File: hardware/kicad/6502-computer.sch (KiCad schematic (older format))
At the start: 35 parts, among them J1 Conn_02x20_Odd_Even, J2 Barrel_Jack, J3 Conn_02x02_Odd_Even, J4 Conn_02x06_Odd_Even, J5 Conn_02x06_Odd_Even, J6 Conn_01x06_Female, SW1 SW_SPDT, SW2 SW_SPDT, SW3 SW_Push, U1 W65C02SxP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

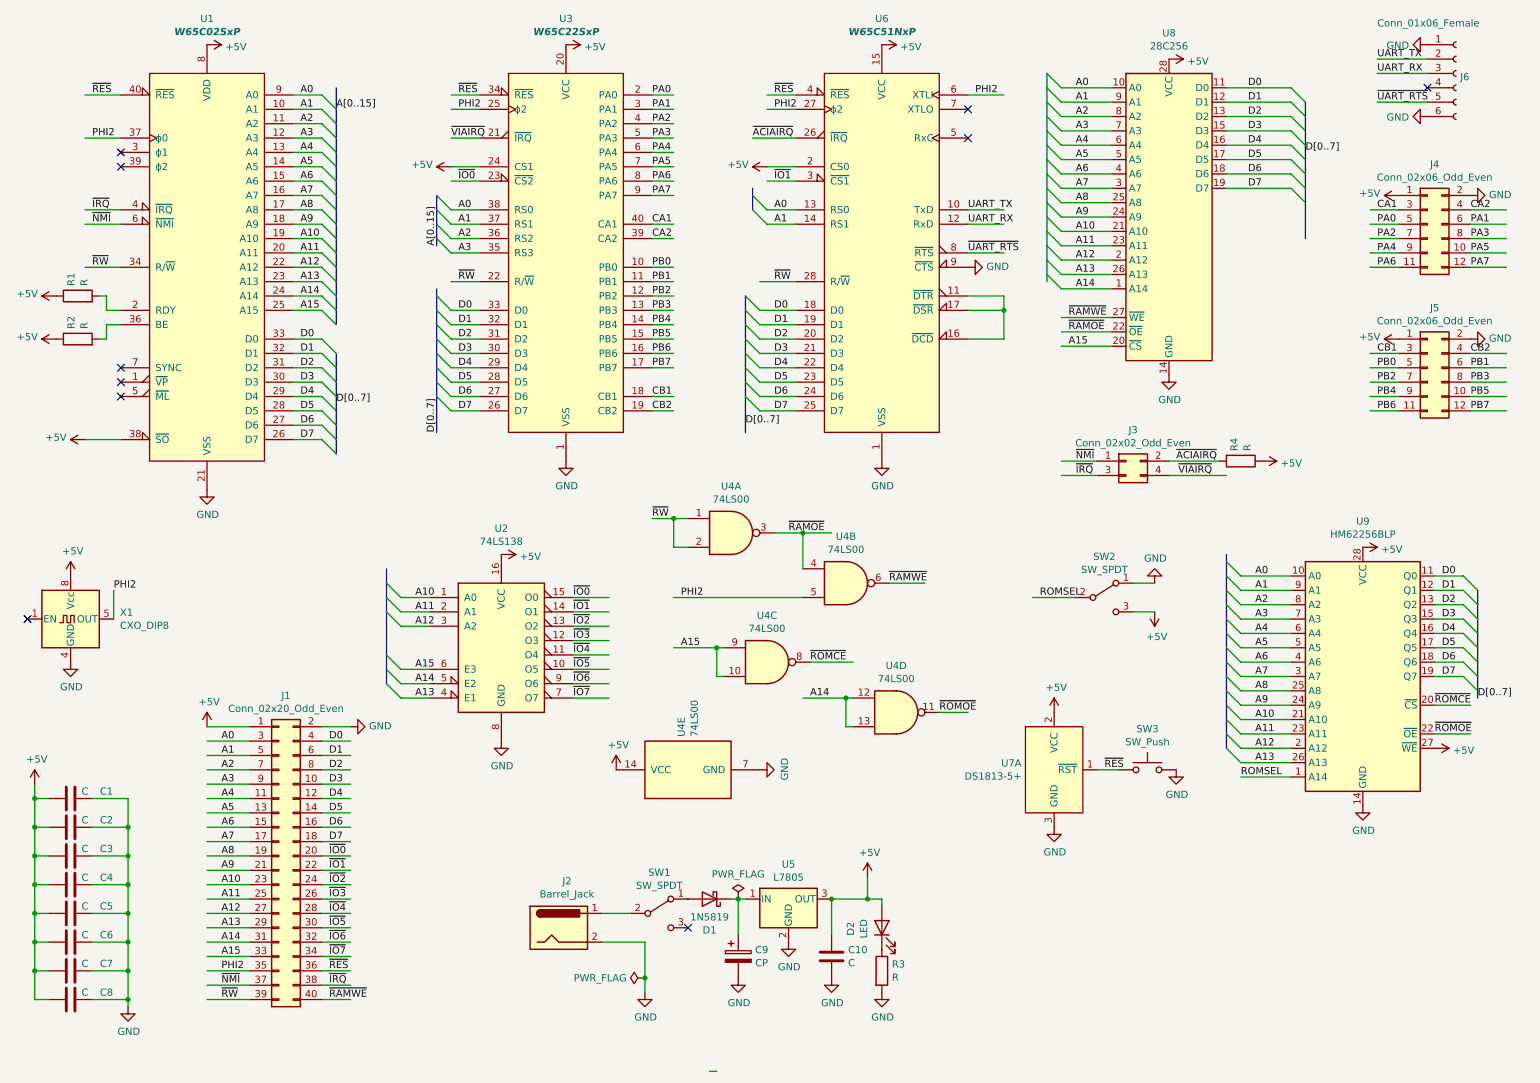
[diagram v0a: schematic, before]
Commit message: add component values
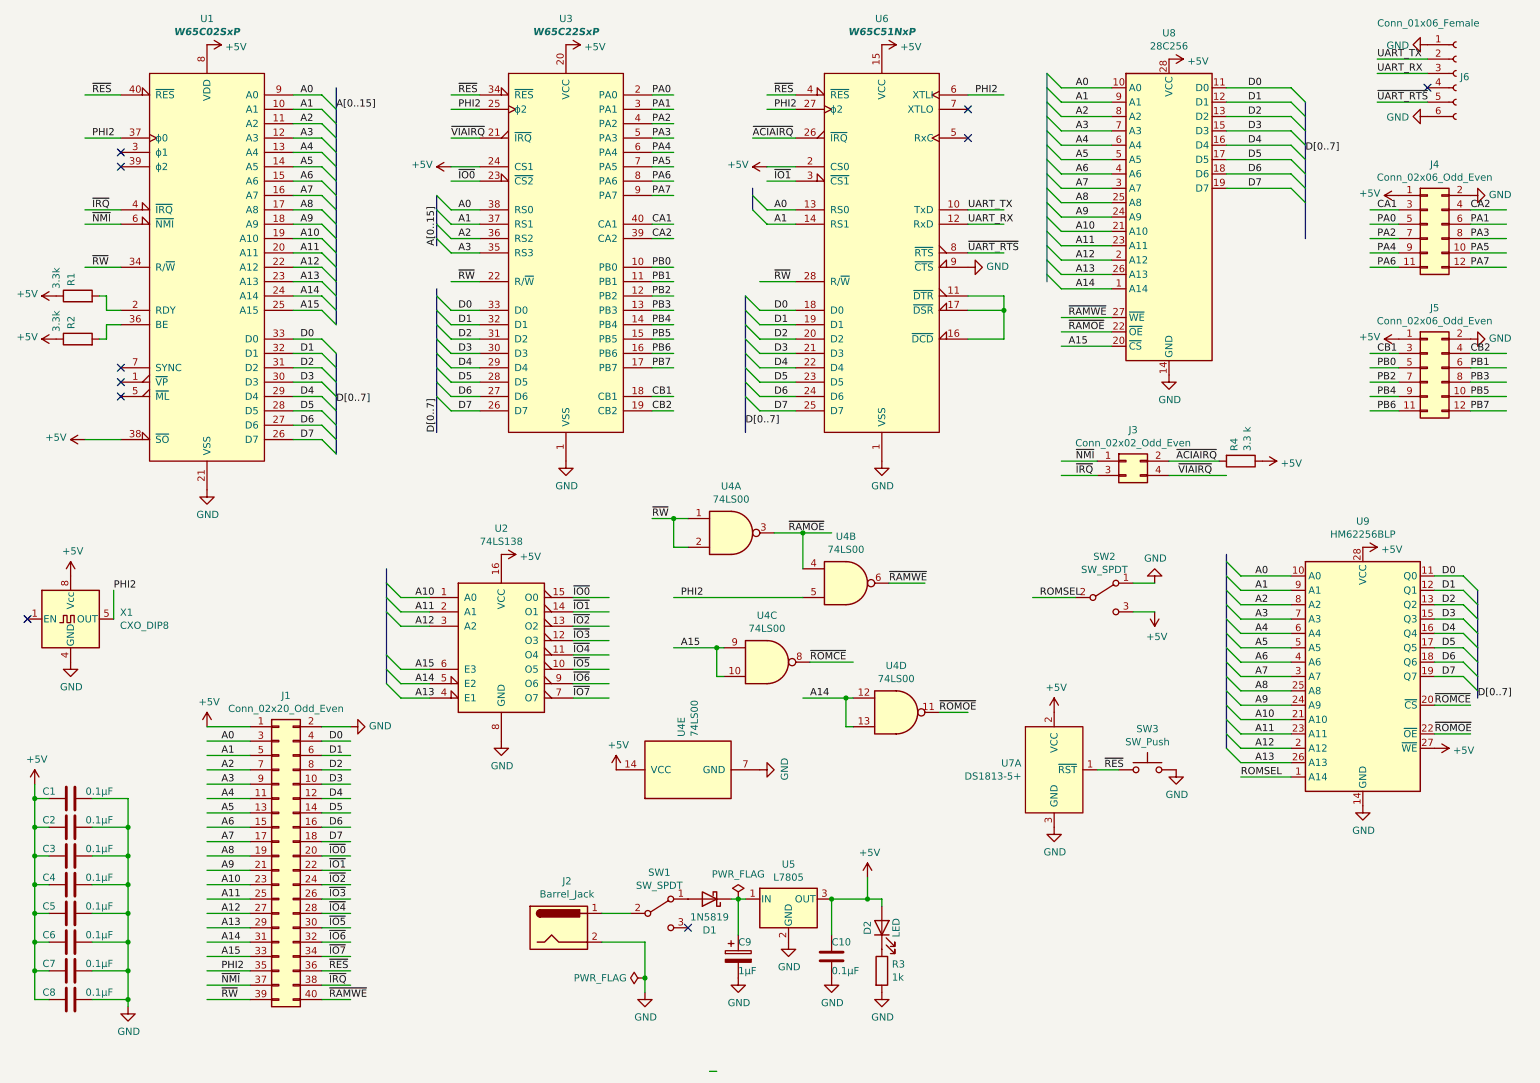
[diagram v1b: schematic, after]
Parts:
- C1, C10, C2, C3, C4, C5, C6, C7, C8: value C -> 0.1µF
- C9: value CP -> 1µF
- R1, R2: value R -> 3.3k
- R3: value R -> 1k
- R4: value R -> 3.3 k
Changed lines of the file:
@@
 U 1 1 61089D2F
 P 6250 7100
-F 0 "C10" H 6365 7146 50  0000 L CNN
-F 1 "C" H 6365 7055 50  0000 L CNN
+F 0 "C10" H 6250 7200 50  0000 L CNN
+F 1 "0.1µF" H 6250 7000 50  0000 L CNN
 F 2 "Capacitor_THT:C_Disc_D5.0mm_W2.5mm_P2.50mm" H 6288 6950 50  0001 C CNN
 F 3 "~" H 6250 7100 50  0001 C CNN
@@
 U 1 1 612507AF
 P 6600 6900
-F 0 "D2" H 6593 7117 50  0000 C CNN
-F 1 "LED" H 6593 7026 50  0000 C CNN
+F 0 "D2" H 6600 7000 50  0000 C CNN
+F 1 "LED" H 6600 6800 50  0000 C CNN
 F 2 "LED_THT:LED_D5.0mm" H 6600 6900 50  0001 C CNN
 F 3 "~" H 6600 6900 50  0001 C CNN
@@
 P 6600 7200
 F 0 "R3" H 6670 7246 50  0000 L CNN
-F 1 "R" H 6670 7155 50  0000 L CNN
+F 1 "1k" H 6670 7155 50  0000 L CNN
 F 2 "Resistor_THT:R_Axial_DIN0207_L6.3mm_D2.5mm_P10.16mm_Horizontal" V 6530 7200 50  0001 C CNN
 F 3 "~" H 6600 7200 50  0001 C CNN
@@
 P 1000 2800
 F 0 "R2" H 1070 2846 50  0000 L CNN
-F 1 "R" H 1070 2755 50  0000 L CNN
+F 1 "3.3k" H 1050 2950 50  0000 L CNN
 F 2 "Resistor_THT:R_Axial_DIN0207_L6.3mm_D2.5mm_P10.16mm_Horizontal" V 930 2800 50  0001 C CNN
 F 3 "~" H 1000 2800 50  0001 C CNN
@@
 P 1000 2500
 F 0 "R1" H 1070 2546 50  0000 L CNN
-F 1 "R" H 1070 2455 50  0000 L CNN
+F 1 "3.3k" H 1050 2650 50  0000 L CNN
 F 2 "Resistor_THT:R_Axial_DIN0207_L6.3mm_D2.5mm_P10.16mm_Horizontal" V 930 2500 50  0001 C CNN
 F 3 "~" H 1000 2500 50  0001 C CNN
@@
 ~ACIAIRQ
 $Comp
-L Device:R R4
-U 1 1 6218038F
-P 9100 3650
-F 0 "R4" H 9030 3604 50  0000 R CNN
-F 1 "R" H 9030 3695 50  0000 R CNN
-F 2 "Resistor_THT:R_Axial_DIN0207_L6.3mm_D2.5mm_P10.16mm_Horizontal" V 9030 3650 50  0001 C CNN
-F 3 "~" H 9100 3650 50  0001 C CNN
-	1    9100 3650
-	0    1    1    0
-$EndComp
-$Comp
 L Connector_Generic:Conn_02x02_Odd_Even J3
 U 1 1 62141DBF
@@
 $EndComp
 $Comp
-L power:GND #PWR0141
-U 1 1 62A2C16E
-P 1350 7450
-F 0 "#PWR0141" H 1350 7200 50  0001 C CNN
-F 1 "GND" H 1355 7277 50  0000 C CNN
-F 2 "" H 1350 7450 50  0001 C CNN
-F 3 "" H 1350 7450 50  0001 C CNN
-	1    1350 7450
-	1    0    0    -1
-$EndComp
-$Comp
-L Device:C C1
-U 1 1 62A8A6E5
-P 950 6000
-F 0 "C1" V 900 6250 50  0000 C CNN
-F 1 "C" V 900 6100 50  0000 C CNN
-F 2 "Capacitor_THT:C_Disc_D5.0mm_W2.5mm_P2.50mm" H 988 5850 50  0001 C CNN
-F 3 "~" H 950 6000 50  0001 C CNN
-	1    950  6000
-	0    1    1    0
-$EndComp
-$Comp
-L Device:C C2
-U 1 1 62AEDE99
-P 950 6200
-F 0 "C2" V 900 6450 50  0000 C CNN
-F 1 "C" V 900 6300 50  0000 C CNN
-F 2 "Capacitor_THT:C_Disc_D5.0mm_W2.5mm_P2.50mm" H 988 6050 50  0001 C CNN
-F 3 "~" H 950 6200 50  0001 C CNN
-	1    950  6200
-	0    1    1    0
-$EndComp
-$Comp
-L Device:C C4
-U 1 1 62BCA622
-P 950 6600
-F 0 "C4" V 900 6850 50  0000 C CNN
-F 1 "C" V 900 6700 50  0000 C CNN
-F 2 "Capacitor_THT:C_Disc_D5.0mm_W2.5mm_P2.50mm" H 988 6450 50  0001 C CNN
-F 3 "~" H 950 6600 50  0001 C CNN
-	1    950  6600
-	0    1    1    0
-$EndComp
-$Comp
 L Device:C C5
 U 1 1 62BCB673
 P 950 6800
-F 0 "C5" V 900 7050 50  0000 C CNN
-F 1 "C" V 900 6900 50  0000 C CNN
+F 0 "C5" V 900 6650 50  0000 C CNN
+F 1 "0.1µF" V 900 7000 50  0000 C CNN
 F 2 "Capacitor_THT:C_Disc_D5.0mm_W2.5mm_P2.50mm" H 988 6650 50  0001 C CNN
 F 3 "~" H 950 6800 50  0001 C CNN
@@
 U 1 1 62BCC41D
 P 950 7000
-F 0 "C6" V 900 7250 50  0000 C CNN
-F 1 "C" V 900 7100 50  0000 C CNN
+F 0 "C6" V 900 6850 50  0000 C CNN
+F 1 "0.1µF" V 900 7200 50  0000 C CNN
 F 2 "Capacitor_THT:C_Disc_D5.0mm_W2.5mm_P2.50mm" H 988 6850 50  0001 C CNN
 F 3 "~" H 950 7000 50  0001 C CNN
@@
 $EndComp
 $Comp
-L Device:C C7
-U 1 1 62BCD16B
-P 950 7200
-F 0 "C7" V 900 7450 50  0000 C CNN
-F 1 "C" V 900 7300 50  0000 C CNN
-F 2 "Capacitor_THT:C_Disc_D5.0mm_W2.5mm_P2.50mm" H 988 7050 50  0001 C CNN
-F 3 "~" H 950 7200 50  0001 C CNN
-	1    950  7200
-	0    1    1    0
-$EndComp
-$Comp
 L Device:C C8
 U 1 1 62BEB99E
 P 950 7400
-F 0 "C8" V 900 7650 50  0000 C CNN
-F 1 "C" V 900 7500 50  0000 C CNN
+F 0 "C8" V 900 7250 50  0000 C CNN
+F 1 "0.1µF" V 900 7600 50  0000 C CNN
 F 2 "Capacitor_THT:C_Disc_D5.0mm_W2.5mm_P2.50mm" H 988 7250 50  0001 C CNN
 F 3 "~" H 950 7400 50  0001 C CNN
@@
 	0    1    1    0
 $EndComp
-$Comp
-L Device:C C3
-U 1 1 62B14BC7
-P 950 6400
-F 0 "C3" V 900 6650 50  0000 C CNN
-F 1 "C" V 900 6500 50  0000 C CNN
-F 2 "Capacitor_THT:C_Disc_D5.0mm_W2.5mm_P2.50mm" H 988 6250 50  0001 C CNN
-F 3 "~" H 950 6400 50  0001 C CNN
-	1    950  6400
-	0    1    1    0
-$EndComp
-Wire Wire Line
-	1100 6000 1350 6000
-Wire Wire Line
-	1350 6000 1350 6200
-Wire Wire Line
-	1100 6200 1350 6200
-Connection ~ 1350 6200
-Wire Wire Line
-	1350 6200 1350 6400
-Wire Wire Line
-	1100 6400 1350 6400
-Connection ~ 1350 6400
-Wire Wire Line
-	1350 6400 1350 6600
-Wire Wire Line
-	1100 6600 1350 6600
-Connection ~ 1350 6600
-Wire Wire Line
-	1350 6600 1350 6800
-Wire Wire Line
-	1100 6800 1350 6800
-Connection ~ 1350 6800
-Wire Wire Line
-	1350 6800 1350 7000
-Wire Wire Line
-	1100 7000 1350 7000
-Connection ~ 1350 7000
-Wire Wire Line
-	1350 7000 1350 7200
-Wire Wire Line
-	1100 7200 1350 7200
-Connection ~ 1350 7200
-Wire Wire Line
-	1350 7200 1350 7400
-Wire Wire Line
-	1100 7400 1350 7400
-Connection ~ 1350 7400
-Wire Wire Line
-	1350 7400 1350 7450
 Wire Wire Line
 	700  5900 700  6000
@@
 	1    0    0    -1
 $EndComp
-$Comp
-L Device:CP C9
-U 1 1 61088D22
-P 5600 7100
-F 0 "C9" H 5718 7146 50  0000 L CNN
-F 1 "CP" H 5718 7055 50  0000 L CNN
-F 2 "Capacitor_THT:C_Radial_D4.0mm_H7.0mm_P1.50mm" H 5638 6950 50  0001 C CNN
-F 3 "~" H 5600 7100 50  0001 C CNN
-	1    5600 7100
-	1    0    0    -1
-$EndComp
 Connection ~ 6250 6700
 Wire Wire Line
@@
 	0    1    1    0
 $EndComp
+$Comp
+L Device:CP C9
+U 1 1 61088D22
+P 5600 7100
+F 0 "C9" H 5600 7200 50  0000 L CNN
+F 1 "1µF" H 5600 7000 50  0000 L CNN
+F 2 "Capacitor_THT:C_Radial_D4.0mm_H7.0mm_P1.50mm" H 5638 6950 50  0001 C CNN
+F 3 "~" H 5600 7100 50  0001 C CNN
+	1    5600 7100
+	1    0    0    -1
+$EndComp
+$Comp
+L Device:C C4
+U 1 1 62BCA622
+P 950 6600
+F 0 "C4" V 900 6450 50  0000 C CNN
+F 1 "0.1µF" V 900 6800 50  0000 C CNN
+F 2 "Capacitor_THT:C_Disc_D5.0mm_W2.5mm_P2.50mm" H 988 6450 50  0001 C CNN
+F 3 "~" H 950 6600 50  0001 C CNN
+	1    950  6600
+	0    1    1    0
+$EndComp
+$Comp
+L Device:C C3
+U 1 1 62B14BC7
+P 950 6400
+F 0 "C3" V 900 6250 50  0000 C CNN
+F 1 "0.1µF" V 900 6600 50  0000 C CNN
+F 2 "Capacitor_THT:C_Disc_D5.0mm_W2.5mm_P2.50mm" H 988 6250 50  0001 C CNN
+F 3 "~" H 950 6400 50  0001 C CNN
+	1    950  6400
+	0    1    1    0
+$EndComp
+$Comp
+L Device:C C2
+U 1 1 62AEDE99
+P 950 6200
+F 0 "C2" V 900 6050 50  0000 C CNN
+F 1 "0.1µF" V 900 6400 50  0000 C CNN
+F 2 "Capacitor_THT:C_Disc_D5.0mm_W2.5mm_P2.50mm" H 988 6050 50  0001 C CNN
+F 3 "~" H 950 6200 50  0001 C CNN
+	1    950  6200
+	0    1    1    0
+$EndComp
+$Comp
+L Device:C C1
+U 1 1 62A8A6E5
+P 950 6000
+F 0 "C1" V 900 5850 50  0000 C CNN
+F 1 "0.1µF" V 900 6200 50  0000 C CNN
+F 2 "Capacitor_THT:C_Disc_D5.0mm_W2.5mm_P2.50mm" H 988 5850 50  0001 C CNN
+F 3 "~" H 950 6000 50  0001 C CNN
+	1    950  6000
+	0    1    1    0
+$EndComp
+Wire Bus Line
+	9550 1150 9550 2100
+Wire Bus Line
+	3150 4400 3150 5200
+Wire Bus Line
+	7750 950  7750 2400
 Wire Bus Line
 	5700 1750 5700 1900
 Wire Bus Line
+	9000 4300 9000 5650
+Wire Bus Line
 	3500 1800 3500 2150
 Wire Bus Line
-	2800 2900 2800 3600
+	10750 4550 10750 5300
 Wire Bus Line
-	3150 4400 3150 5200
-Wire Bus Line
-	9550 1150 9550 2100
-Wire Bus Line
-	10750 4550 10750 5300
+	2800 1050 2800 2700
 Wire Bus Line
 	3500 2450 3500 3450
@@
 	5650 2500 5650 3450
 Wire Bus Line
-	9000 4300 9000 5650
-Wire Bus Line
-	7750 950  7750 2400
-Wire Bus Line
-	2800 1050 2800 2700
+	2800 2900 2800 3600
+Wire Wire Line
+	1350 7400 1350 7450
+Connection ~ 1350 7400
+Wire Wire Line
+	1100 7400 1350 7400
+Wire Wire Line
+	1350 7200 1350 7400
+Connection ~ 1350 7200
+Wire Wire Line
+	1350 7000 1350 7200
+Connection ~ 1350 7000
+Wire Wire Line
+	1100 7000 1350 7000
+Wire Wire Line
+	1350 6800 1350 7000
+Connection ~ 1350 6800
+Wire Wire Line
+	1100 6800 1350 6800
+Wire Wire Line
+	1350 6600 1350 6800
+Connection ~ 1350 6600
+Wire Wire Line
+	1100 6600 1350 6600
+Wire Wire Line
+	1350 6400 1350 6600
+Connection ~ 1350 6400
+Wire Wire Line
+	1100 6400 1350 6400
+Wire Wire Line
+	1350 6200 1350 6400
+Connection ~ 1350 6200
+Wire Wire Line
+	1100 6200 1350 6200
+Wire Wire Line
+	1350 6000 1350 6200
+Wire Wire Line
+	1100 6000 1350 6000
+$Comp
+L power:GND #PWR0141
+U 1 1 62A2C16E
+P 1350 7450
+F 0 "#PWR0141" H 1350 7200 50  0001 C CNN
+F 1 "GND" H 1355 7277 50  0000 C CNN
+F 2 "" H 1350 7450 50  0001 C CNN
+F 3 "" H 1350 7450 50  0001 C CNN
+	1    1350 7450
+	1    0    0    -1
+$EndComp
+Wire Wire Line
+	1100 7200 1350 7200
+$Comp
+L Device:C C7
+U 1 1 62BCD16B
+P 950 7200
+F 0 "C7" V 900 7050 50  0000 C CNN
+F 1 "0.1µF" V 900 7400 50  0000 C CNN
+F 2 "Capacitor_THT:C_Disc_D5.0mm_W2.5mm_P2.50mm" H 988 7050 50  0001 C CNN
+F 3 "~" H 950 7200 50  0001 C CNN
+	1    950  7200
+	0    1    1    0
+$EndComp
+$Comp
+L Device:R R4
+U 1 1 6218038F
+P 9100 3650
+F 0 "R4" H 9030 3604 50  0000 R CNN
+F 1 "3.3 k" H 9030 3695 50  0000 R CNN
+F 2 "Resistor_THT:R_Axial_DIN0207_L6.3mm_D2.5mm_P10.16mm_Horizontal" V 9030 3650 50  0001 C CNN
+F 3 "~" H 9100 3650 50  0001 C CNN
+	1    9100 3650
+	0    1    1    0
+$EndComp
 $EndSCHEMATC

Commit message: add PDF schematic, parts list
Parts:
- R4: value 3.3 k -> 3.3k
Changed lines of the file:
@@
 encoding utf-8
 Sheet 1 1
-Title ""
-Date ""
+Title "6502 Computer"
+Date "2021-08-22"
 Rev ""
-Comp ""
-Comment1 ""
+Comp "Michael Billington"
+Comment1 "https://github.com/mike42/6502-computer"
 Comment2 ""
 Comment3 ""
@@
 	0    1    1    0
 $EndComp
-Wire Bus Line
-	9550 1150 9550 2100
-Wire Bus Line
-	3150 4400 3150 5200
-Wire Bus Line
-	7750 950  7750 2400
-Wire Bus Line
-	5700 1750 5700 1900
-Wire Bus Line
-	9000 4300 9000 5650
-Wire Bus Line
-	3500 1800 3500 2150
-Wire Bus Line
-	10750 4550 10750 5300
-Wire Bus Line
-	2800 1050 2800 2700
-Wire Bus Line
-	3500 2450 3500 3450
-Wire Bus Line
-	5650 2500 5650 3450
-Wire Bus Line
-	2800 2900 2800 3600
 Wire Wire Line
 	1350 7400 1350 7450
@@
 P 9100 3650
 F 0 "R4" H 9030 3604 50  0000 R CNN
-F 1 "3.3 k" H 9030 3695 50  0000 R CNN
+F 1 "3.3k" H 9030 3695 50  0000 R CNN
 F 2 "Resistor_THT:R_Axial_DIN0207_L6.3mm_D2.5mm_P10.16mm_Horizontal" V 9030 3650 50  0001 C CNN
 F 3 "~" H 9100 3650 50  0001 C CNN
@@
 	0    1    1    0
 $EndComp
+Wire Bus Line
+	5700 1750 5700 1900
+Wire Bus Line
+	3500 1800 3500 2150
+Wire Bus Line
+	2800 2900 2800 3600
+Wire Bus Line
+	3150 4400 3150 5200
+Wire Bus Line
+	9550 1150 9550 2100
+Wire Bus Line
+	10750 4550 10750 5300
+Wire Bus Line
+	3500 2450 3500 3450
+Wire Bus Line
+	5650 2500 5650 3450
+Wire Bus Line
+	9000 4300 9000 5650
+Wire Bus Line
+	7750 950  7750 2400
+Wire Bus Line
+	2800 1050 2800 2700
 $EndSCHEMATC
